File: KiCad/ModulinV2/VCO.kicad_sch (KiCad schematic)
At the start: 40 parts, among them SW4 SW_SPDT_MSM

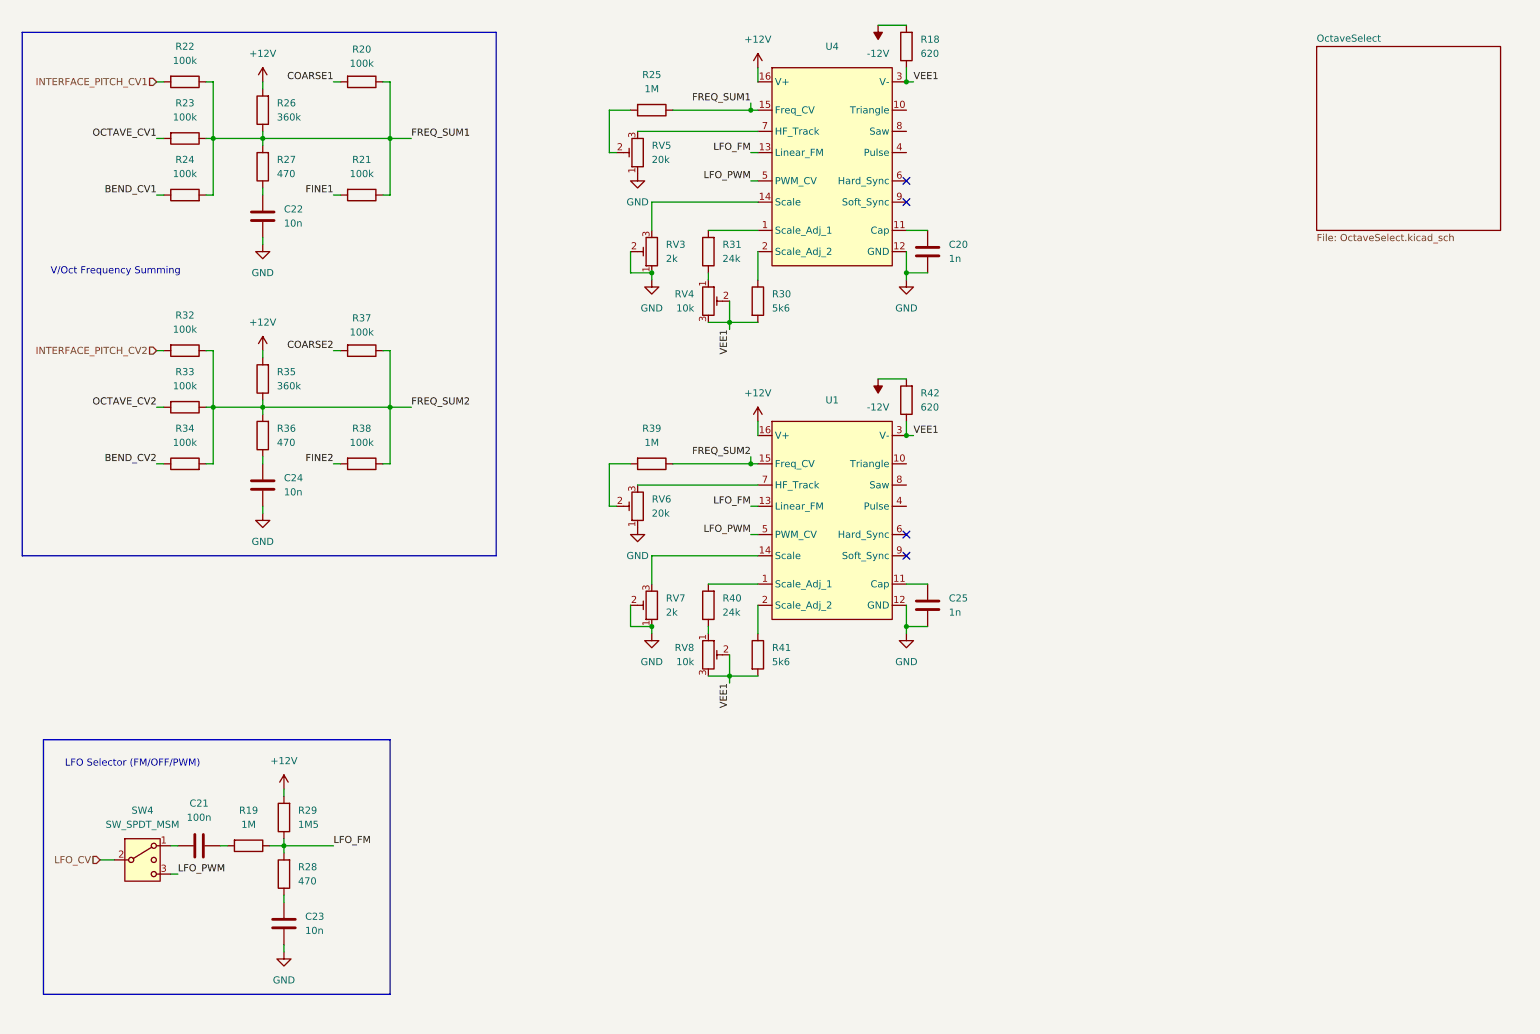
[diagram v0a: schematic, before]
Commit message: Finished 1.0 of the VCO and started making the waveform select module
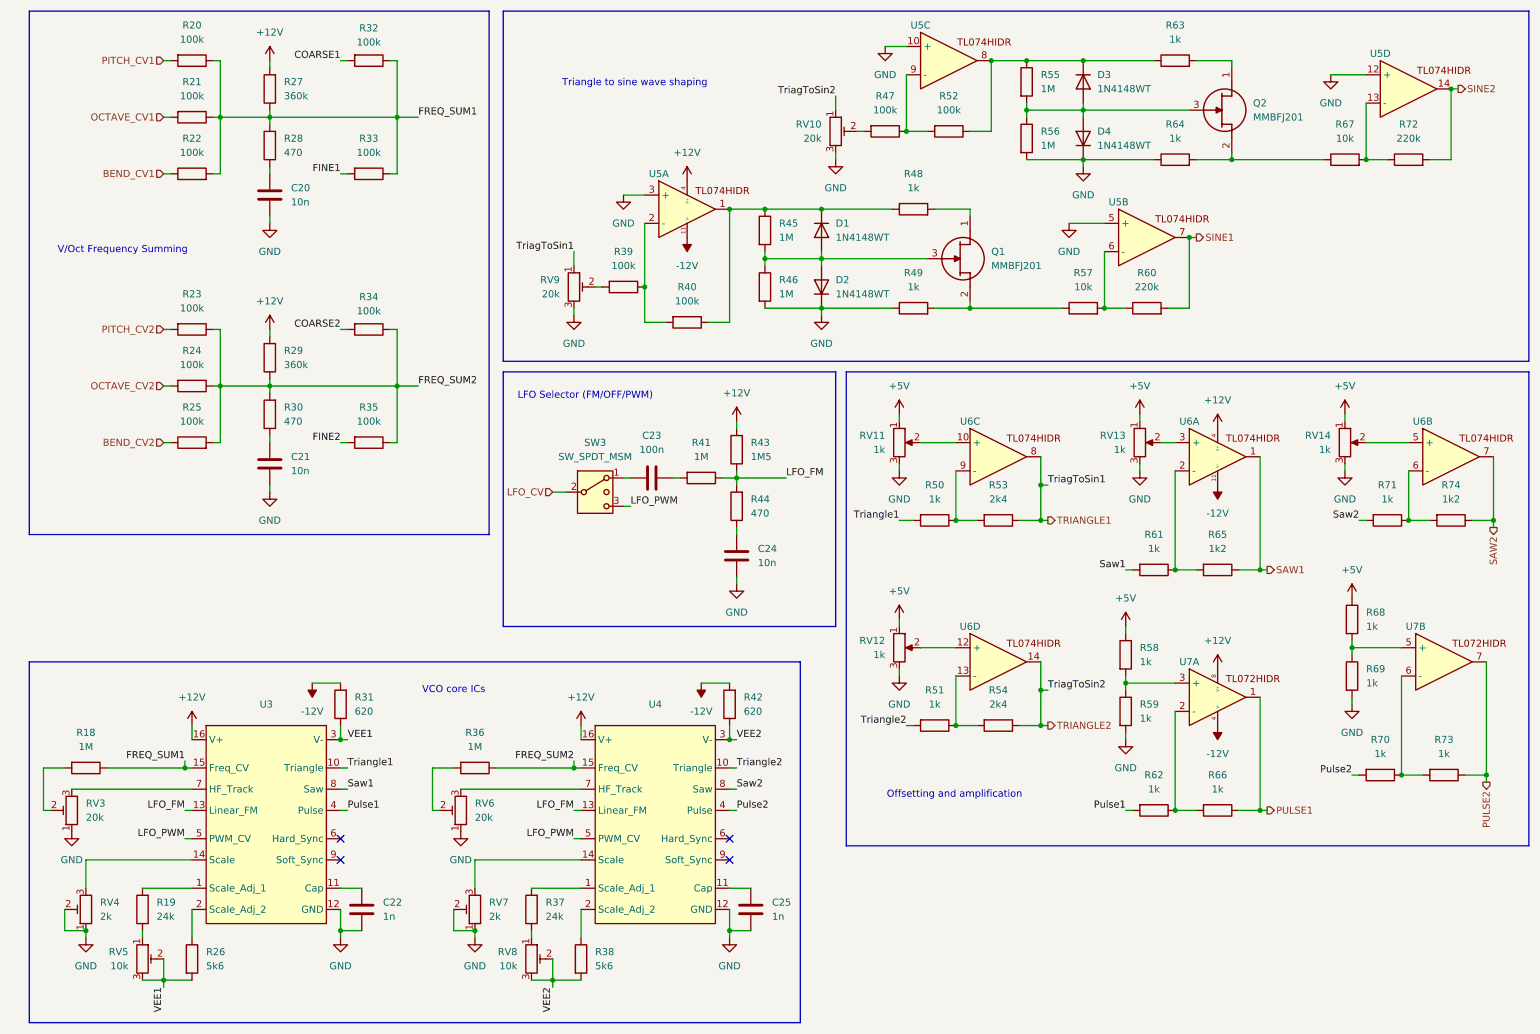
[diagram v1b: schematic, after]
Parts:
- added D1, D2, D3, D4: 1N4148WT, Diode_SMD:D_SOD-523, symbol Diode:1N4148WT
- added Q1, Q2: MMBFJ201, SOT95P240X120-3N, symbol MMBFJ201:MMBFJ201
- added R39, R40, R47, R52: 100k, symbol Device:R
- added R45, R46, R55, R56: 1M, symbol Device:R
- added R48, R49, R50, R51, R58, R59, R61, R62, R63, R64, R66, R68, R69, R70, R71, R73: 1k, symbol Device:R
- added R53, R54: 2k4, symbol Device:R
- added R57, R67: 10k, symbol Device:R
- added R60, R72: 220k, symbol Device:R
- added R65, R74: 1k2, symbol Device:R
- added RV10, RV9: 20k, symbol Device:R_Potentiometer_Trim
- added RV11, RV12, RV13, RV14: 1k, symbol Device:R_Potentiometer
- added U5, U6: ~, symbol TL074HIDR:TL074HIDRx4
- added U7: ~, symbol TL072HIDR:TL072HIDRx2
- renumbered C22 to C20, C24 to C21, C20 to C22, C21 to C23, C23 to C24, R25 to R18, R31 to R19, R22 to R20, R23 to R21, R24 to R22, R32 to R23, R33 to R24, R34 to R25, R30 to R26, R26 to R27, R27 to R28, R35 to R29, R36 to R30, R18 to R31, R20 to R32, R21 to R33, R37 to R34, R38 to R35, R39 to R36, R40 to R37, R41 to R38, R19 to R41, R29 to R43, R28 to R44, RV5 to RV3, RV3 to RV4, RV4 to RV5, SW4 to SW3, U4 to U3, U1 to U4
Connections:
- net +12V: now also U5.4 (V+), U6.4 (V+), U7.8 (V+)
- net -12V: now also U5.11 (V-), U6.11 (V-), U7.4 (V-)
- net GND: now also D2.1 (K), D4.1 (K), R46.2, R49.1, R56.2, R59.2, R64.1, R69.2, RV10.3, RV11.3, RV12.3, RV13.3, RV14.3, RV9.3, U5.10 (+), U5.12 (+), U5.3 (+), U5.5 (+)
- net VEE1: no longer R38.2, R42.1, RV8.2, RV8.3, U4.3 (V-)
- net Triangle2: now reaches U4.10 (Triangle)
- net Triangle2: now also R51.2
- net Pulse2: now reaches U4.4 (Pulse)
- net Pulse2: now also R70.2
- net Saw2: now reaches U4.8 (Saw)
- net Saw2: now also R71.2
- net Triangle1: now reaches U3.10 (Triangle)
- net Triangle1: now also R50.2
- net Pulse1: now reaches U3.4 (Pulse)
- net Pulse1: now also R62.2
- net Saw1: now reaches U3.8 (Saw)
- net Saw1: now also R61.2
- net INTERFACE_PITCH_CV1 renamed PITCH_CV1
- net INTERFACE_PITCH_CV2 renamed PITCH_CV2
- new net: RV14.2, U6.5 (+)
- new net: R71.1, R74.2, U6.6 (-)
- new net: Q2.1 (D), R63.2
- new net: Q2.2 (S), R64.2, R67.1
- new net: D3.2 (A), D4.2 (A), Q2.3 (G), R55.2, R56.1
- new net: D3.1 (K), R52.1, R55.1, R63.1, U5.8
- new net: R62.1, R66.2, U7.2 (-)
- new net: R58.2, R59.1, U7.3 (+)
- new net: R47.2, RV10.2
- new net: RV11.2, U6.10 (+)
- new net: R50.1, R53.2, U6.9 (-)
- new net: R39.2, RV9.2
- new net: D1.1 (K), R40.1, R45.1, R48.1, U5.1
- new net: R39.1, R40.2, U5.2 (-)
- new net: R67.2, R72.1, U5.13 (-)
- new net: R70.1, R73.2, U7.6 (-)
- new net: D1.2 (A), D2.2 (A), Q1.3 (G), R45.2, R46.1
- new net: RV12.2, U6.12 (+)
- new net: R51.1, R54.2, U6.13 (-)
- new net: R68.2, R69.1, U7.5 (+)
- new net: Q1.2 (S), R49.2, R57.1
- new net: R57.2, R60.1, U5.6 (-)
- new net: R61.1, R65.2, U6.2 (-)
- new net: RV13.2, U6.3 (+)
- new net: R47.1, R52.2, U5.9 (-)
- new net: Q1.1 (D), R48.2
- new net +5V: R58.1, R68.1, RV11.1, RV12.1, RV13.1, RV14.1
- new net PULSE1: R66.1, U7.1
- new net PULSE2: R73.1, U7.7
- new net SAW1: R65.1, U6.1
- new net SAW2: R74.1, U6.7
- new net SINE1: R60.2, U5.7
- new net SINE2: R72.2, U5.14
- new net TRIANGLE1: R53.1, RV9.1, U6.8
- new net TRIANGLE2: R54.1, RV10.1, U6.14
- new net VEE2: R38.2, R42.1, RV8.2, RV8.3, U4.3 (V-)
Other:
- removed sheet OctaveSelect
- note added: "Offsetting and amplification"
- note added: "Triangle to sine wave shaping"
- note added: "VCO core ICs"
- title: (none) -> Voltage Controlled Oscillator
- moved on the sheet: C20, C21, C22, C23, C24, C25, R18, R19, R20, R21, R22, R23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

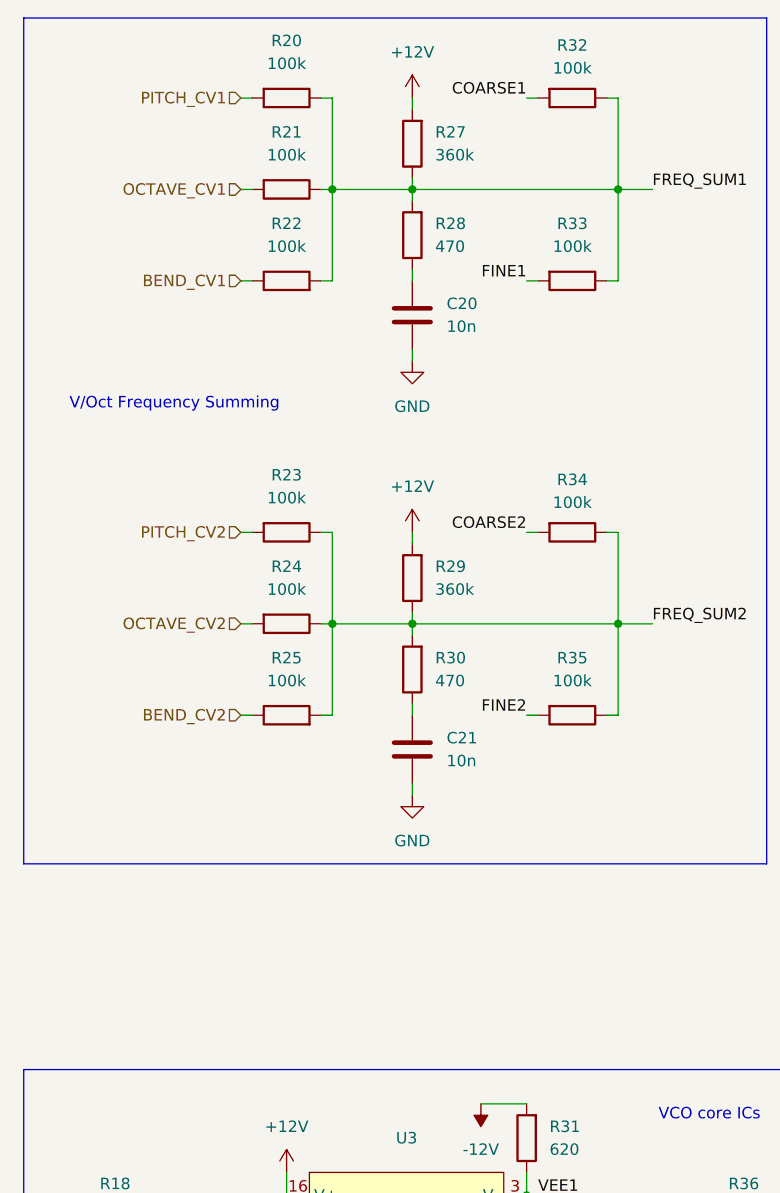
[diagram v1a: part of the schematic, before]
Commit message: Modified Octave selector and started on waveform selection
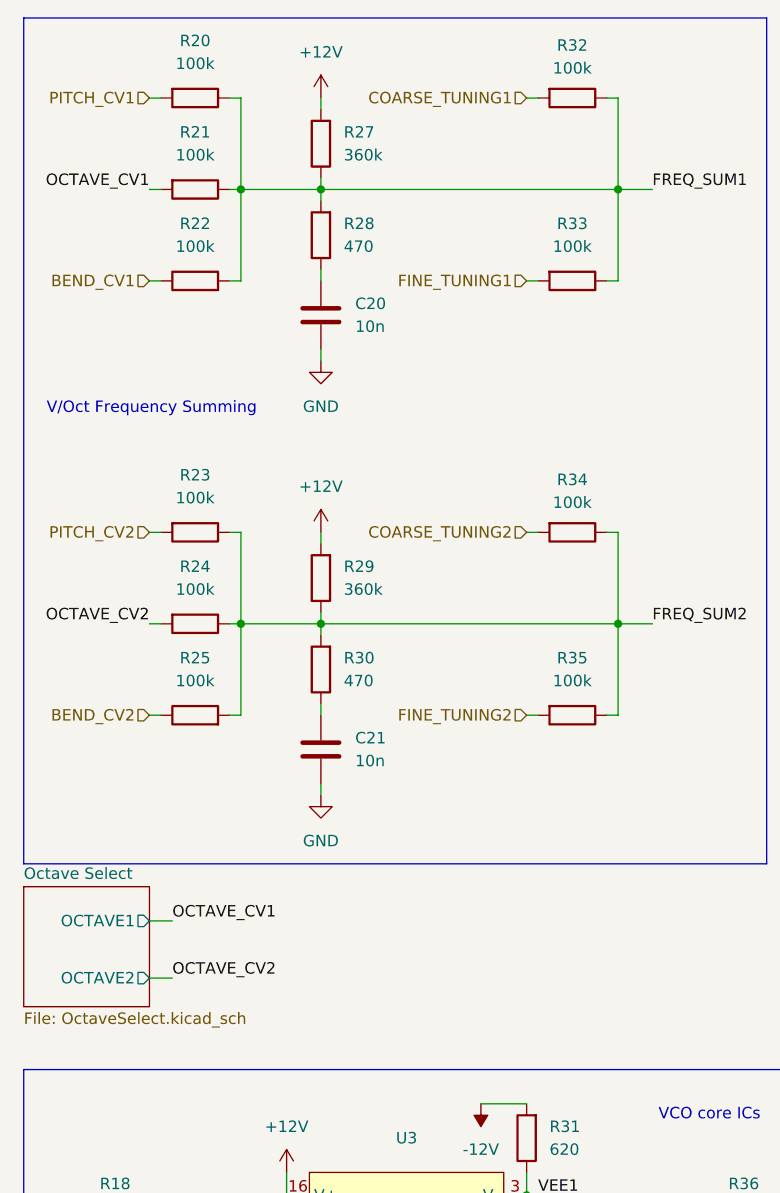
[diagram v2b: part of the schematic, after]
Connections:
- net COARSE1 renamed COARSE_TUNING1
- net COARSE2 renamed COARSE_TUNING2
- net FINE1 renamed FINE_TUNING1
- net FINE2 renamed FINE_TUNING2
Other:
- added sheet Octave Select (OctaveSelect.kicad_sch)
- moved on the sheet: C20, C21, R20, R21, R22, R23, R24, R25, R27, R28, R29, R30

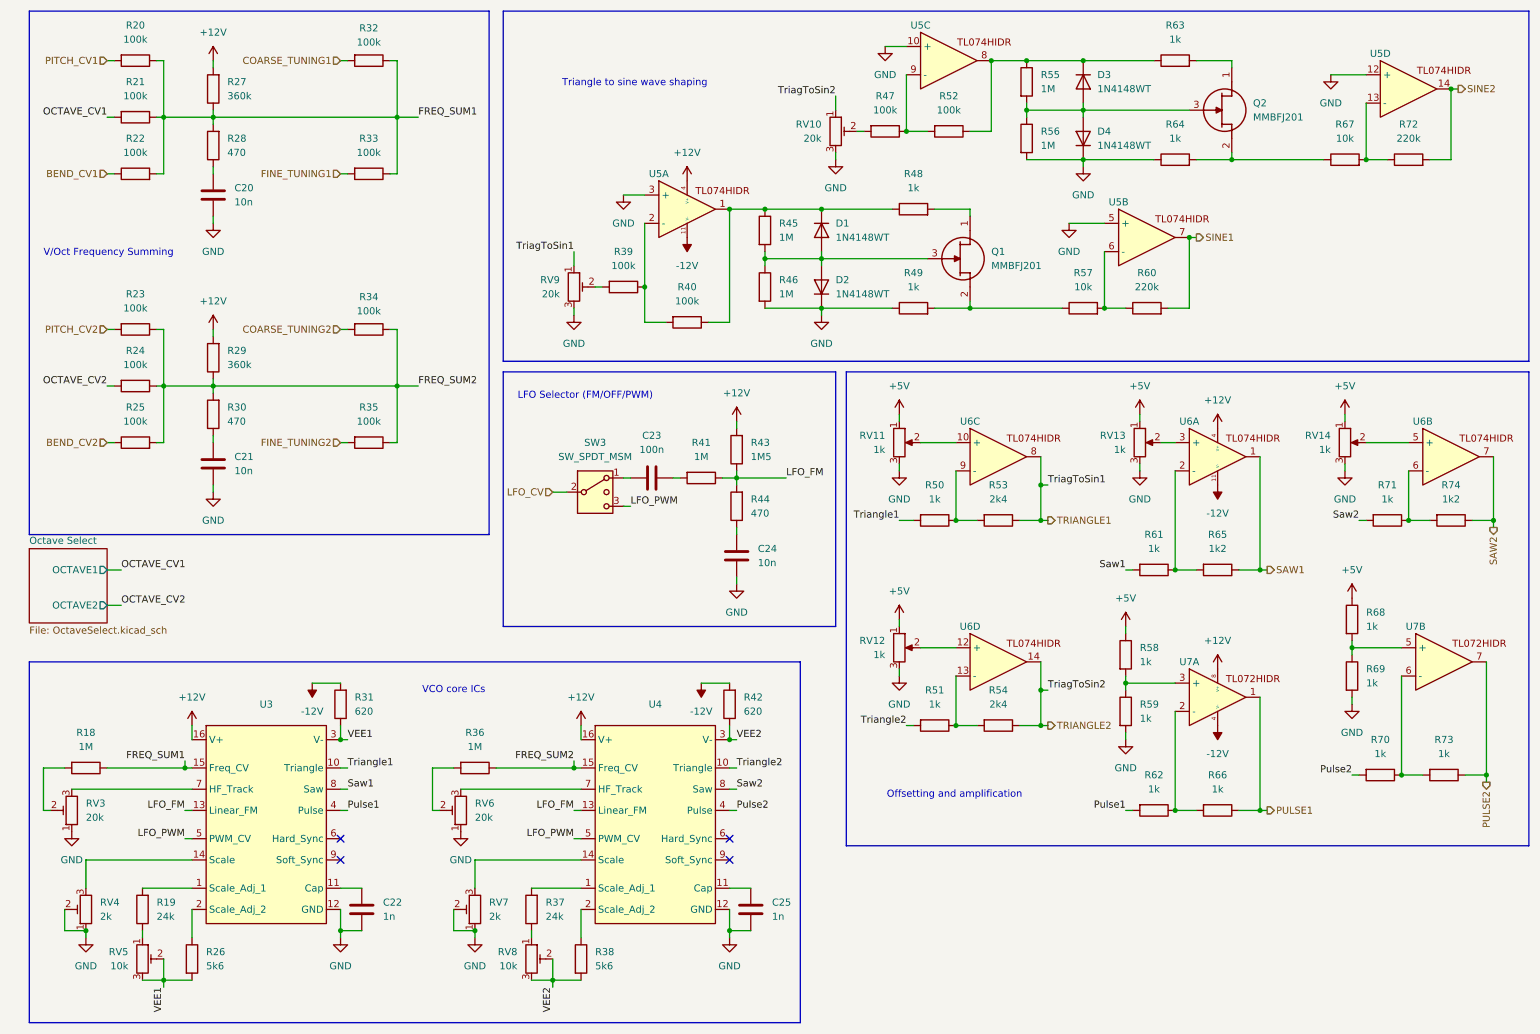
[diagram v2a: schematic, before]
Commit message: Modified USB connection and added LEDs
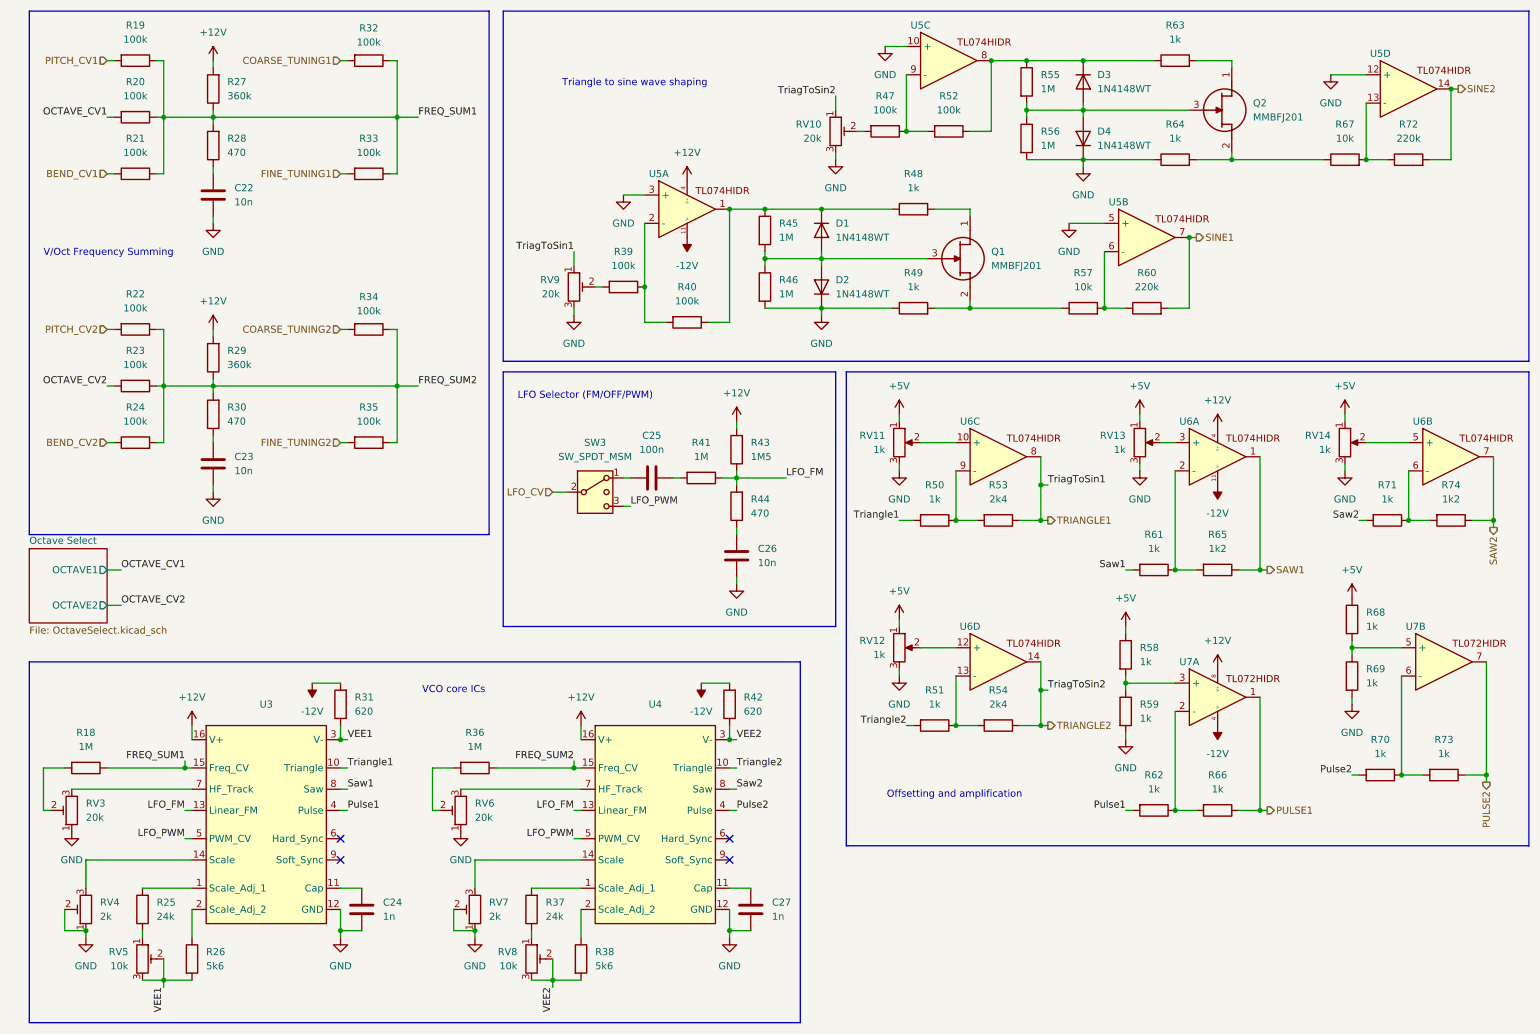
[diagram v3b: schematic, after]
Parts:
- renumbered C20 to C22, C21 to C23, C22 to C24, C23 to C25, C24 to C26, C25 to C27, R20 to R19, R21 to R20, R22 to R21, R23 to R22, R24 to R23, R25 to R24, R19 to R25
